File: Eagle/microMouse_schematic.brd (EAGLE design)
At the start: 80 x 100 mm, 54 parts, among them IC1 DSPIC33FJ64MC804-PT, IC2 L293D, IC3 LM340MP-05, IC5 MC33269D-3.3, X1 +9V

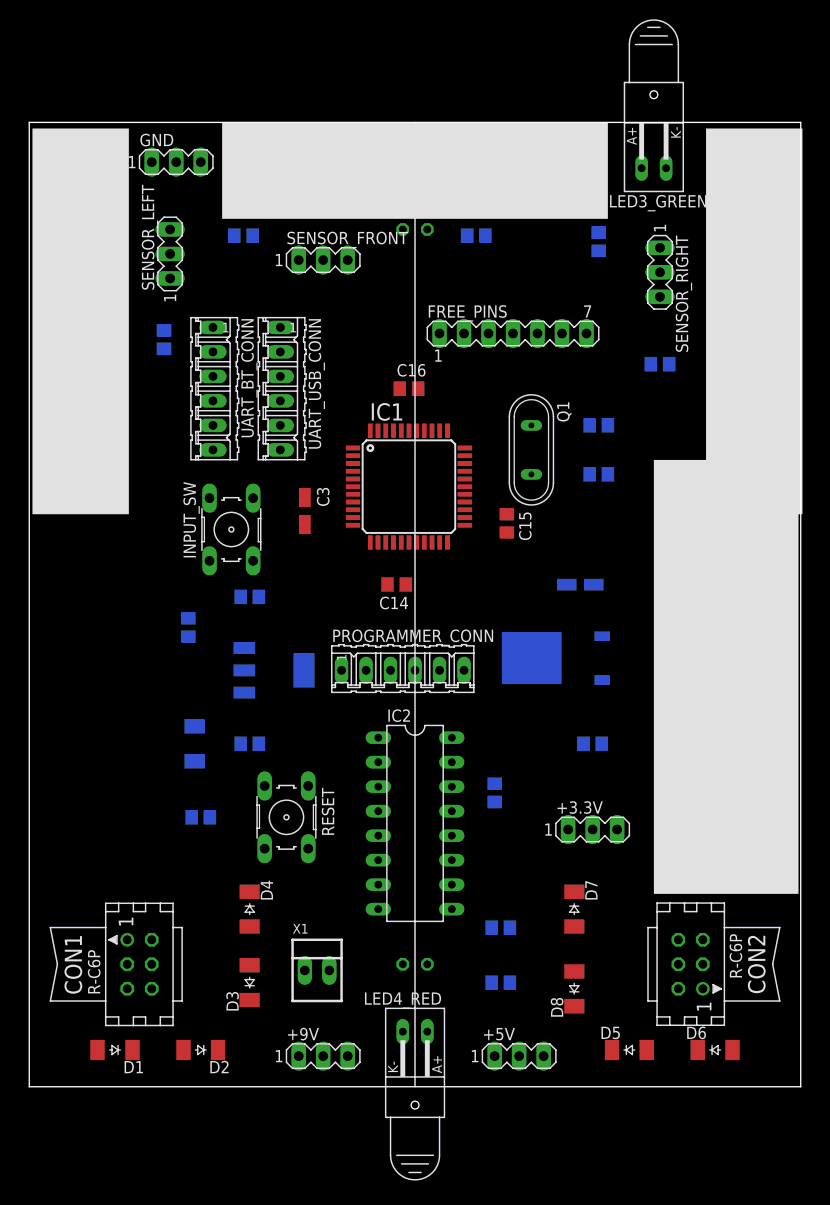
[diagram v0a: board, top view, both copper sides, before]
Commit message: PCB signals routing
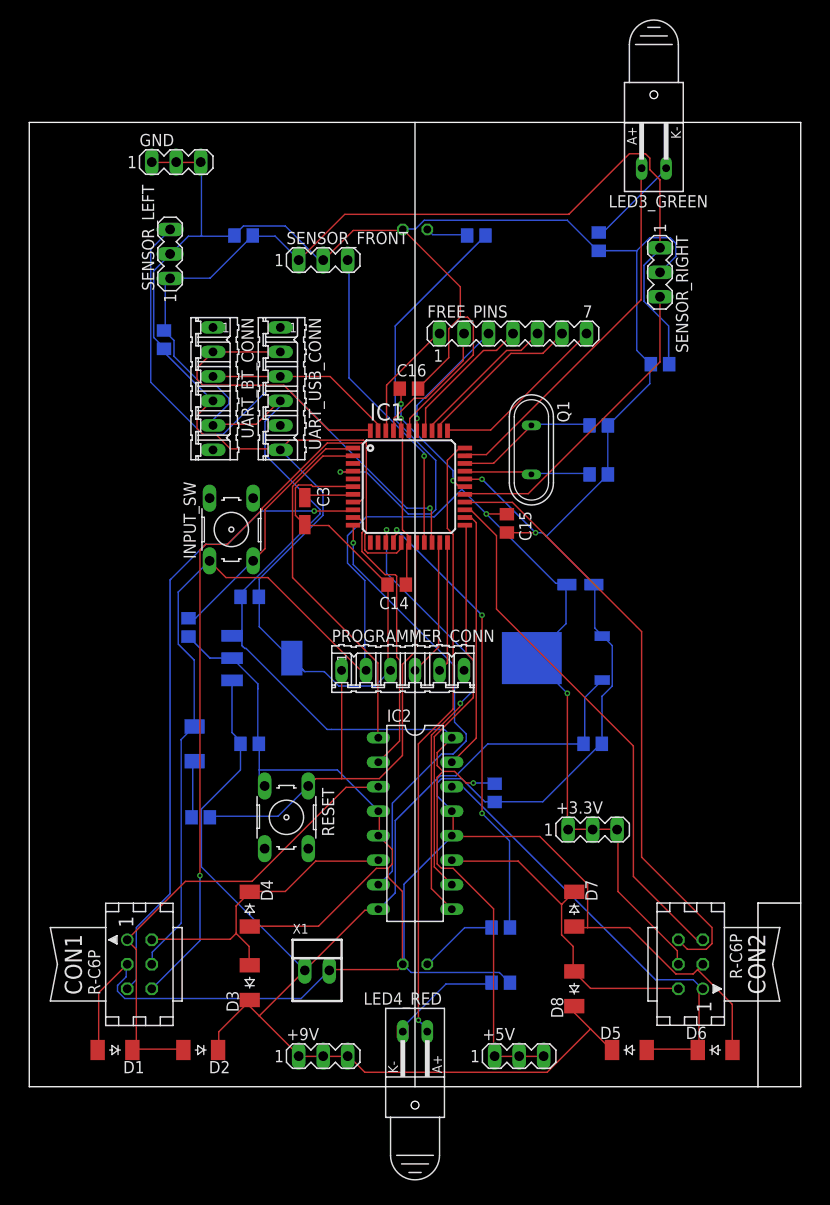
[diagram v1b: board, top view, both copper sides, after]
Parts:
- IC3: value LM340MP-05 -> LM340MP-5.0
- moved IC3 1.80 mm to (24.1, 44.5)
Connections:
- net GND: now also IC3.2
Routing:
- net GND: track 0.00 -> 529.9 mm, vias 0 -> 2
- net +5V: track 0.00 -> 216.2 mm, vias 0 -> 1
- net VDD: track 0.00 -> 195.1 mm, vias 0 -> 5
- net +9V: track 0.00 -> 147.6 mm
- net LM_ENC_CH_A: track 0.00 -> 76.1 mm, vias 0 -> 1
- net LM_ENC_CH_B: track 0.00 -> 66.2 mm, vias 0 -> 1
- net N$15: track 0.00 -> 63.8 mm, vias 0 -> 1
- net RM_ENC_CH_A: track 0.00 -> 63.4 mm
- net ADC_CH_2: track 0.00 -> 58.4 mm, vias 0 -> 1
- net RESET: track 0.00 -> 56.6 mm
- net RM_ENC_CH_B: track 0.00 -> 55.5 mm
- net N$4: track 0.00 -> 50.1 mm
- net N$14: track 0.00 -> 47.5 mm, vias 0 -> 3
- net N$1: track 0.00 -> 47.3 mm, vias 0 -> 1
- net PWM_1_RIGHT_MOTOR: track 0.00 -> 47.1 mm, vias 0 -> 2
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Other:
- outline, holes or cut-outs redrawn

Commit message: add motor & sensor mounts, add GND planes
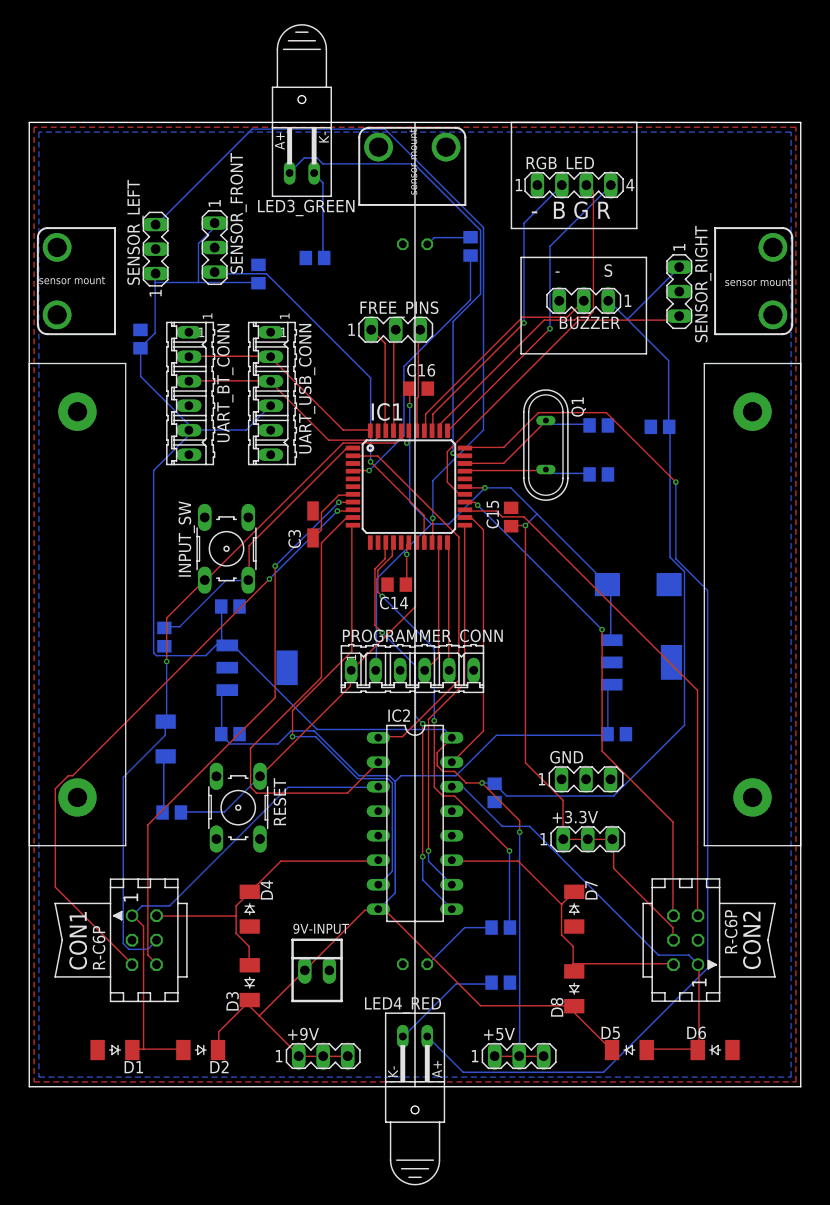
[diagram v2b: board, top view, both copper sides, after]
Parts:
- removed IC5: MC33269D-3.3, linear:DPACK
- added BUZZER: (no value), con-lstb:MA03-1
- added IC4: LM3940IMP-3.3, linear:SOT223
- added RGB_LED: (no value), con-lstb:MA04-1
- added SENS_MNT_F: SENSOR_MOUNT_F, linear:SENSOR_MOUNT
- added SENS_MNT_L: SENSOR_MOUNT_L, linear:SENSOR_MOUNT
- added SENS_MNT_R: SENSOR_MOUNT_R, linear:SENSOR_MOUNT
- added U$1, U$2: MOTOR_MOUNT, linear:MOTOR_MOUNT
- C7: value 10uF Tantalum -> 33uF Tantalum; device rcl:CT3216 -> rcl:CT7343
- FREE_PINS: device con-lstb:MA07-1 -> con-lstb:MA03-1
- moved GND 76.8 mm to (57.7, 31.9)
- moved LED3_GREEN 36.5 mm to (28.3, 102.4)
- moved R4 29.5 mm to (29.6, 85.9), turned to 0 degrees
- moved FREE_PINS 12.2 mm to (38.0, 78.5)
- moved SENSOR_FRONT 11.3 mm to (19.2, 87.0), turned to 270 degrees
- moved C11 6.50 mm to (65.4, 68.4)
- moved C7 6.00 mm to (63.1, 52.1)
- moved RESET 5.10 mm to (21.7, 28.9)
- moved C8 4.28 mm to (23.8, 84.3), turned to 90 degrees
- moved R5 3.04 mm to (14.8, 28.4)
- moved D9 3.04 mm to (14.1, 36.1)
- moved SENSOR_RIGHT 2.83 mm to (67.4, 82.5)
- moved R3 2.69 mm to (14.0, 46.6)
- moved C12 2.69 mm to (60.9, 36.6)
- moved CON1 2.55 mm to (11.9, 15.2)
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- renumbered X1 to 9V-INPUT
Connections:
- net +5V: now also BUZZER.1
- net +9V: now also IC4.1; no longer IC5.3
- net GND: now also BUZZER.3, IC4.2, IC4.4, RGB_LED.1, SENS_MNT_F.P$1, SENS_MNT_F.P$2, SENS_MNT_L.P$1, SENS_MNT_L.P$2, SENS_MNT_R.P$1, SENS_MNT_R.P$2, U$1.P$1, U$1.P$2, U$2.P$1, U$2.P$2; no longer IC5.1
- net N$16: now also RGB_LED.4; no longer FREE_PINS.7
- net N$18: now also RGB_LED.3; no longer FREE_PINS.6
- net N$20: now also RGB_LED.2; no longer FREE_PINS.5
- net N$21: now also BUZZER.2; no longer FREE_PINS.4
- net VDD: now also IC4.3; no longer IC5.2
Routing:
- net GND: track 529.9 -> 0.00 mm, vias 2 -> 0
- net N$15: track 63.8 -> 113.2 mm
- net N$1: track 47.3 -> 28.4 mm
- net ADC_CH_2: track 58.4 -> 77.2 mm
- net +5V: track 216.2 -> 234.6 mm, vias 1 -> 2
- net LM_H_BRDG_DIR_1: track 29.4 -> 47.6 mm
- net LM_ENC_CH_A: track 76.1 -> 58.0 mm, vias 1 -> 2
- net N$18: track 17.2 -> 34.9 mm
- net RESET: track 56.6 -> 40.8 mm
- net N$20: track 15.5 -> 31.0 mm, vias 0 -> 1
- net N$16: track 18.6 -> 32.5 mm, vias 0 -> 1
- net RM_ENC_CH_A: track 63.4 -> 52.4 mm, vias 0 -> 2
- net +9V: track 147.6 -> 137.0 mm
- net N$9: track 38.6 -> 49.2 mm, vias 0 -> 1
- net UART2_TX: track 30.7 -> 22.1 mm
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- added copper zone on layer 1, net GND
- added copper zone on layer 16, net GND
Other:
- outline, holes or cut-outs redrawn
- board text added: "- B G R"
- board text added: "- S"
- board text added: "1"
